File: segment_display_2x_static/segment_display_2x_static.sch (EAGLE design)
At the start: 12 parts, among them IC1 74HC595D, IC2 74HC595D

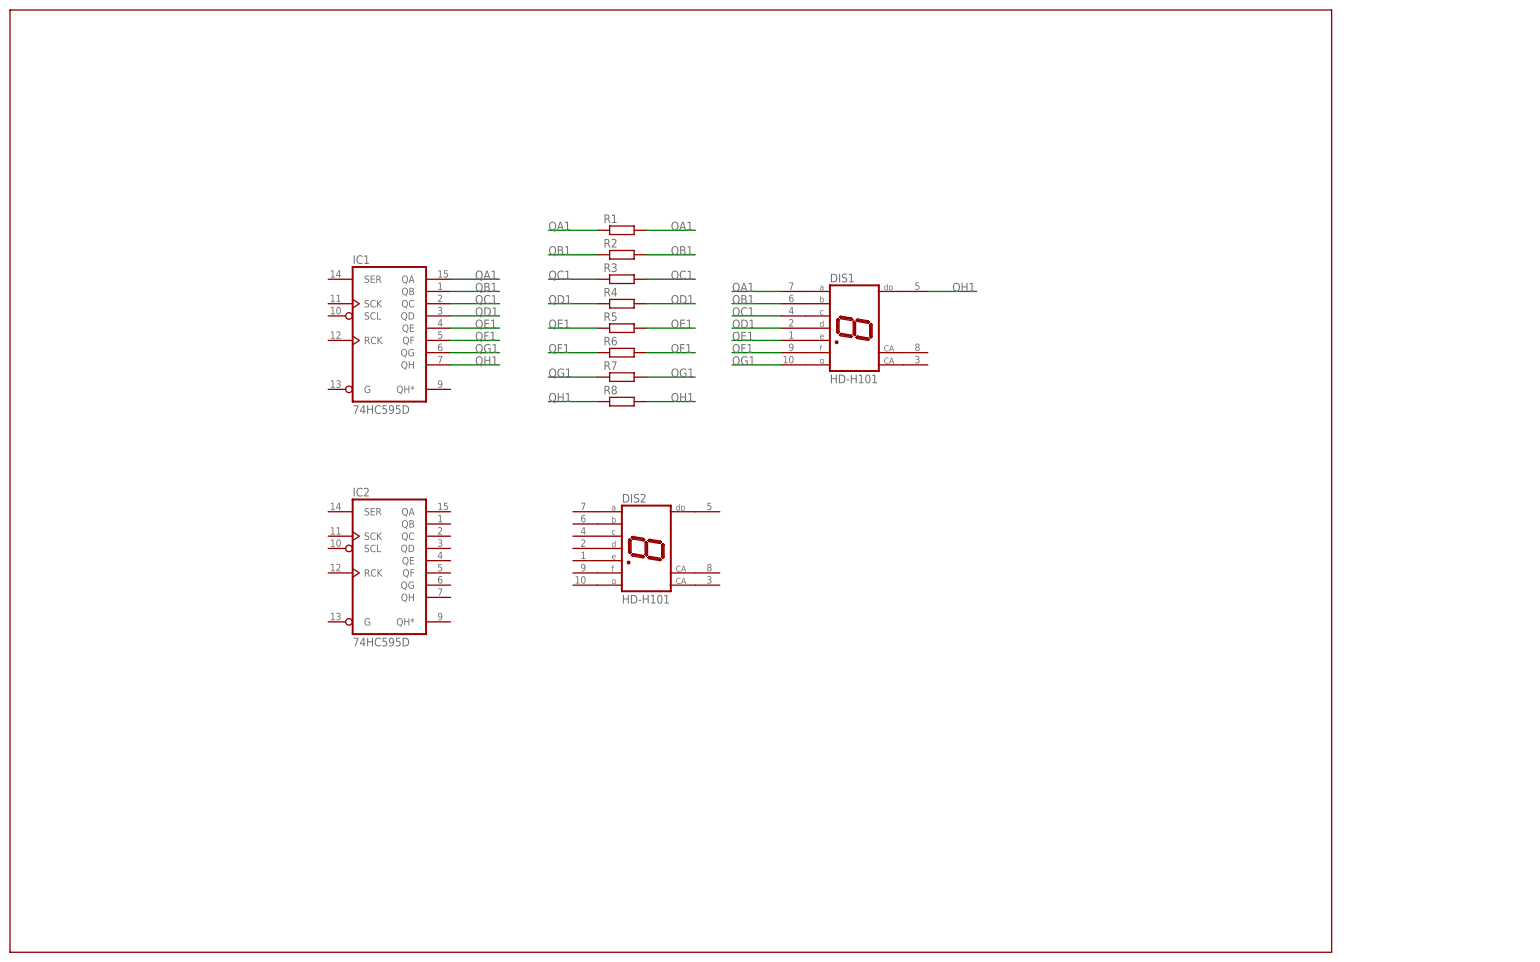
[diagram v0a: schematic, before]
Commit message: added segment_display_2x_static
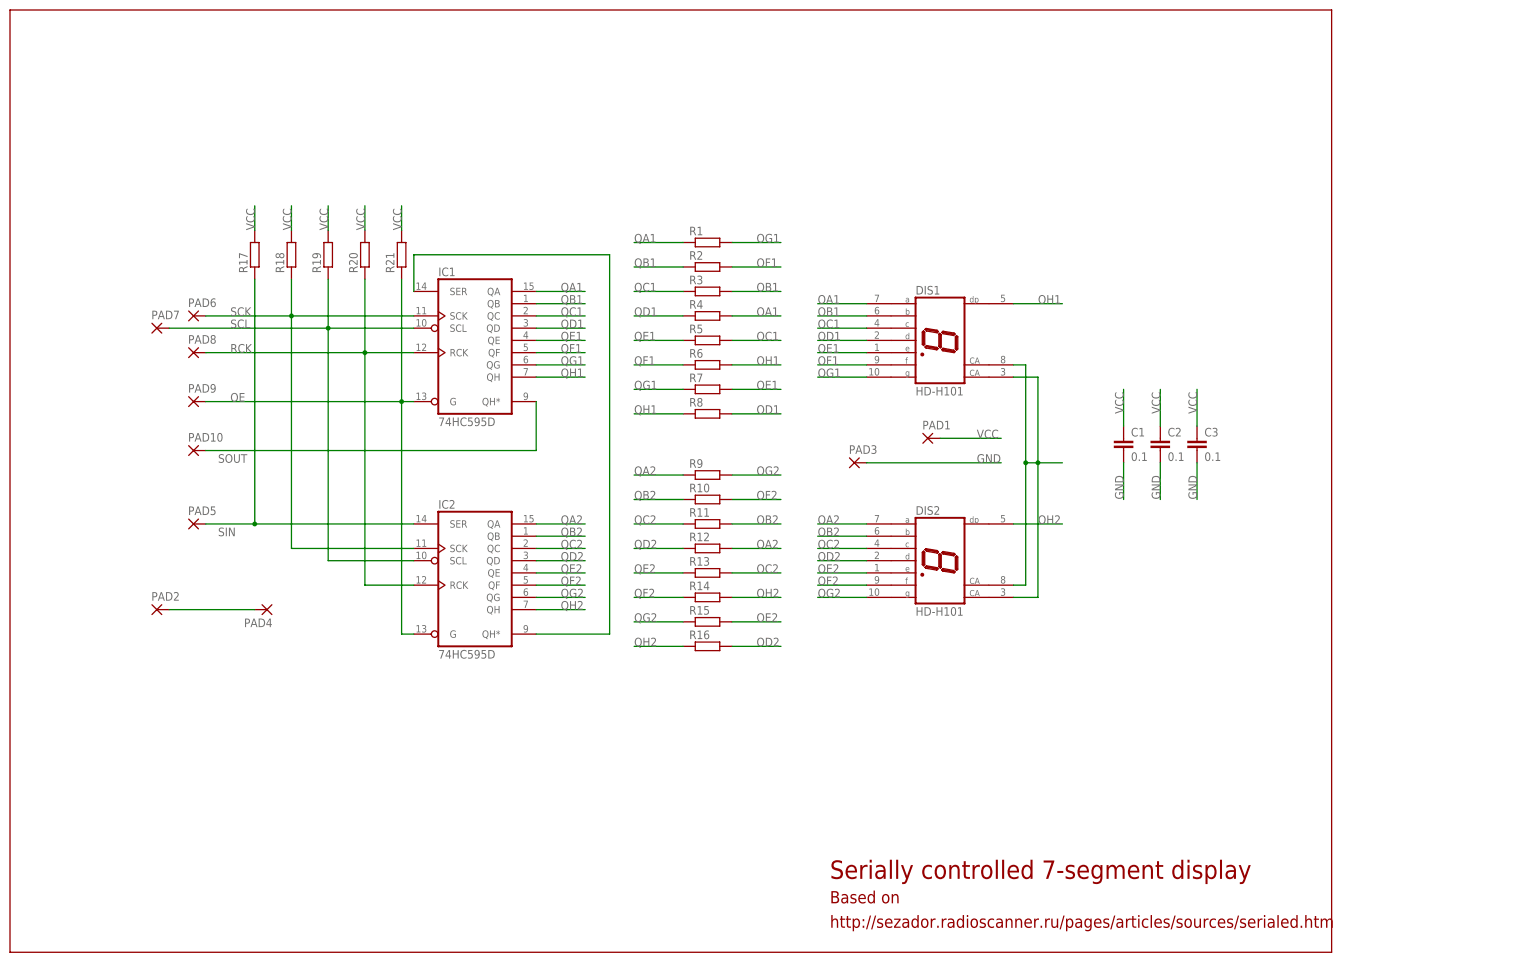
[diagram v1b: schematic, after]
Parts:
- added C1, C2, C3: 0.1, rcl:C-EUC0805
- added PAD1, PAD10, PAD2, PAD3, PAD4, PAD5, PAD6, PAD7, PAD8, PAD9: (no value), wirepad:1,6/0,8
- added R10, R11, R12, R13, R14, R15, R16, R17, R18, R19, R20, R21, R9: (no value), rcl:R-EU_R0805
- R1, R2, R3, R4, R5, R6, R7, R8: device rcl:R-EU_R0603 -> rcl:R-EU_R0805
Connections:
- new net GND: C1.2, C2.2, C3.2, PAD3.P
- new net LINK: IC1A.SER, IC2A.QH*
- new net OA2: DIS2.A, R12.2
- new net OB2: DIS2.B, R11.2
- new net OC2: DIS2.C, R13.2
- new net OD2: DIS2.D, R16.2
- new net OE: IC1A.G, IC2A.G, PAD9.P, R21.1
- new net OE2: DIS2.E, R15.2
- new net OF2: DIS2.F, R10.2
- new net OG2: DIS2.G, R9.2
- new net OH2: DIS2.DP, R14.2
- new net QA2: IC2A.QA, R9.1
- new net QB2: IC2A.QB, R10.1
- new net QC2: IC2A.QC, R11.1
- new net QD2: IC2A.QD, R12.1
- new net QE2: IC2A.QE, R13.1
- new net QF2: IC2A.QF, R14.1
- new net QG2: IC2A.QG, R15.1
- new net QH2: IC2A.QH, R16.1
- new net RCK: IC1A.RCK, IC2A.RCK, PAD8.P, R20.1
- new net RET: PAD2.P, PAD4.P
- new net SCK: IC1A.SCK, IC2A.SCK, PAD6.P, R18.1
- new net SCL: IC1A.SCL, IC2A.SCL, PAD7.P, R19.1
- new net SIN: IC2A.SER, PAD5.P, R17.1
- new net SOUT: IC1A.QH*, PAD10.P
- new net VCC: C1.1, C2.1, C3.1, DIS1.CA, DIS1.CA@1, DIS2.CA, DIS2.CA@1, PAD1.P, R17.2, R18.2, R19.2, R20.2, R21.2
- net OA1: now also R4.2; no longer R1.2
- net OB1: now also R3.2; no longer R2.2
- net OC1: now also R5.2; no longer R3.2
- net OD1: now also R8.2; no longer R4.2
- net OE1: now also R7.2; no longer R5.2
- net OF1: now also R2.2; no longer R6.2
- net OG1: now also R1.2; no longer R7.2
- net OH1: now also R6.2; no longer R8.2
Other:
- note added: "Based on"
- note added: "Serially controlled 7-segment display"
- note added: "http://sezador.radioscanner.ru/pages/articles/sources/serialed.htm"
- moved on the sheet: DIS1, DIS2, IC1, IC2, R1, R2, R3, R4, R5, R6, R7, R8
